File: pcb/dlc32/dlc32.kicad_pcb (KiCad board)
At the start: 2 copper layers, 46 x 79.2 mm, 55 parts, among them IC1 74LV11, IC2 74HCT08, IC3 MAX485E, IC4 AMS1117-3.3, IC5 74HCT04, J1 DOOR1, J10 TO_J7, J11 24V PWR, J12 LED LIGHTING, J13 AIR VALVE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

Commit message: Renumber, delete PCB.
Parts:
- removed C1, C2, C3, C4, C5, C6, C7: 100n, Capacitor_SMD:C_0805_2012Metric
- removed C10, C11, C8, C9: 100u, Capacitor_SMD:CP_Elec_10x10
- removed C12: 100n, Capacitor_SMD:C_0603_1608Metric
- removed D1: SS34, Diode_SMD:D_SMA
- removed IC1: 74LV11, Package_SO:SOIC-14_3.9x8.7mm_P1.27mm
- removed IC2: 74HCT08, Package_SO:SOIC-14_3.9x8.7mm_P1.27mm
- removed IC3: MAX485E, Package_SO:SOIC-8_3.9x4.9mm_P1.27mm
- removed IC4: AMS1117-3.3, Package_TO_SOT_SMD:SOT-223-3_TabPin2
- removed IC5: 74HCT04, Package_SO:SOIC-14_3.9x8.7mm_P1.27mm
- removed J1: DOOR1, Connector_JST:JST_PH_B3B-PH-K_1x03_P2.00mm_Vertical
- removed J10: TO_J7, Connector_JST:JST_XH_B06B-XH-A_1x06_P2.50mm_Vertical
- removed J11: 24V PWR, Connector_JST:JST_PH_B2B-PH-K_1x02_P2.00mm_Vertical
- removed J12: LED LIGHTING, Connector_JST:JST_PH_B2B-PH-K_1x02_P2.00mm_Vertical
- removed J13: AIR VALVE, Connector_JST:JST_PH_B2B-PH-K_1x02_P2.00mm_Vertical
- removed J14: AIMING LASER, Connector_JST:JST_PH_B2B-PH-K_1x02_P2.00mm_Vertical
- removed J15: CHILLER POWER, Connector_JST:JST_PH_B2B-PH-K_1x02_P2.00mm_Vertical
- removed J16: CHILLER SSR, Connector_JST:JST_PH_B2B-PH-K_1x02_P2.00mm_Vertical
- removed J2: DOOR2, Connector_JST:JST_PH_B3B-PH-K_1x03_P2.00mm_Vertical
- removed J3: CHILLER, Connector_JST:JST_PH_B2B-PH-K_1x02_P2.00mm_Vertical
- removed J4: TO_J8, Connector_JST:JST_XH_B06B-XH-A_1x06_P2.50mm_Vertical
- removed J5: POWEROFF, Connector_JST:JST_PH_B3B-PH-K_1x03_P2.00mm_Vertical
- removed J6: Conn_02x04_Odd_Even, Connector_PinSocket_2.54mm:PinSocket_2x04_P2.54mm_Vertical
- removed J7: LASER_AUX, Connector_JST:JST_PH_B5B-PH-K_1x05_P2.00mm_Vertical
- removed J8: LASER, Connector_JST:JST_PH_B5B-PH-K_1x05_P2.00mm_Vertical
- removed J9: CHILLER SERIAL, Connector_JST:JST_PH_B2B-PH-K_1x02_P2.00mm_Vertical
- removed LED1: Enable, LED_SMD:LED_0603_1608Metric
- removed Q1: ZXMN4A06, Package_TO_SOT_SMD:SOT-223-3_TabPin2
- removed R1, R2: 100, Resistor_SMD:R_0603_1608Metric
- removed R10: 120R, Resistor_SMD:R_0603_1608Metric
- removed R11, R13: 10K, Resistor_SMD:R_0603_1608Metric
- removed R12: 22R, Resistor_SMD:R_0603_1608Metric
- removed R3, R4, R5, R9: 1K, Resistor_SMD:R_0603_1608Metric
- removed R6, R7, R8: 5K6, Resistor_SMD:R_0603_1608Metric
- removed REF** (x4): MountingHole_3.2mm_M3, MountingHole:MountingHole_3.2mm_M3
- removed REF**: OSHW-Logo2_7.3x6mm_SilkScreen, Symbol:OSHW-Logo2_7.3x6mm_SilkScreen
- removed U1: MP1584 module, dlc32:MP1584-module
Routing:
- net GND: track 330.3 -> 0.00 mm, vias 6 -> 0
- net +5V: track 180.0 -> 0.00 mm, vias 6 -> 0
- net +3V3: track 135.8 -> 0.00 mm, vias 8 -> 0
- net RX: track 69.3 -> 0.00 mm, vias 4 -> 0
- net Net-(C11-Pad1): track 59.3 -> 0.00 mm
- net Net-(J3-Pad2): track 47.7 -> 0.00 mm, vias 1 -> 0
- net Net-(C10-Pad1): track 45.7 -> 0.00 mm, vias 1 -> 0
- net P2.12: track 44.7 -> 0.00 mm, vias 4 -> 0
- net Net-(J10-Pad4): track 43.2 -> 0.00 mm, vias 2 -> 0
- net Net-(IC2-Pad3): track 38.7 -> 0.00 mm, vias 2 -> 0
- net Net-(D1-Pad2): track 37.3 -> 0.00 mm
- net Net-(IC5-Pad2): track 36.7 -> 0.00 mm, vias 1 -> 0
- net P1.23: track 29.0 -> 0.00 mm, vias 3 -> 0
- net Net-(J2-Pad2): track 28.8 -> 0.00 mm, vias 2 -> 0
- net P4.28: track 23.9 -> 0.00 mm
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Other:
- board outline removed
- board text removed: "Lasersaur"
- board text removed: "https://github.com/bullestock/lasersaur/tree/master/pcb/msksbase"

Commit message: Start PCB.
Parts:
- added C1: 100n, Capacitor_SMD:C_0603_1608Metric, F.Cu at (96.5, 30.5)
- added C2: 100n, Capacitor_SMD:C_0603_1608Metric, F.Cu at (98.0, 47.7)
- added C3: 100n, Capacitor_SMD:C_0603_1608Metric, F.Cu at (98.0, 36.1)
- added C4: 100n, Capacitor_SMD:C_0603_1608Metric, F.Cu at (111.5, 37.3)
- added C5: 100n, Capacitor_SMD:C_0603_1608Metric, F.Cu at (111.5, 25.4)
- added C6: 100u, Capacitor_SMD:CP_Elec_10x10, F.Cu at (199.9, 30.2)
- added C7: 220u, Capacitor_SMD:CP_Elec_10x10, F.Cu at (95.5, 59.4)
- added C8: 100u, Capacitor_SMD:CP_Elec_10x10, F.Cu at (228.7, 101.3)
- added D1: SS34, Diode_SMD:D_SMA, F.Cu at (37.1, 143.3)
- added D2: LED, LED_THT:LED_D5.0mm_Horizontal_O1.27mm_Z3.0mm, F.Cu at (155.9, 47.3)
- added D3: LED, LED_THT:LED_D5.0mm_Horizontal_O1.27mm_Z3.0mm, F.Cu at (155.9, 55.8)
- added D4: LASER_ENABLE, LED_THT:LED_D5.0mm_Horizontal_O1.27mm_Z3.0mm, F.Cu at (155.9, 38.9)
- added D5: 1N4148, Diode_SMD:D_MiniMELF, F.Cu at (79.0, 63.2)
- added D6: LED, LED_THT:LED_D5.0mm_Horizontal_O1.27mm_Z3.0mm, F.Cu at (155.9, 64.3)
- added H1: MountingHole, MountingHole:MountingHole_3.2mm_M3, F.Cu at (78.0, 28.7)
- added H2: MountingHole, MountingHole:MountingHole_3.2mm_M3, F.Cu at (169.4, 28.7)
- added H3: MountingHole, MountingHole:MountingHole_3.2mm_M3, F.Cu at (78.0, 80.5)
- added H4: MountingHole, MountingHole:MountingHole_3.2mm_M3, F.Cu at (169.7, 80.5)
- added IC1: 74HCT08, Package_SO:SOIC-14_3.9x8.7mm_P1.27mm, F.Cu at (109.3, 31.0)
- added IC2: 74HCT04, Package_SO:SOIC-14_3.9x8.7mm_P1.27mm, F.Cu at (109.4, 42.9)
- added J1: DOOR1, Connector_JST:JST_XH_B4B-XH-A_1x04_P2.50mm_Vertical, F.Cu at (77.3, 37.3)
- added J10: VALVE/CHILLER SSR PWR, Connector_JST:JST_XH_B2B-XH-A_1x02_P2.50mm_Vertical, F.Cu at (186.2, 31.0)
- added J11: Conn_01x02, Connector_JST:JST_XH_B2B-XH-A_1x02_P2.50mm_Vertical, F.Cu at (199.4, 51.1)
- added J12: Conn_01x03, Connector_PinHeader_2.54mm:PinHeader_1x03_P2.54mm_Vertical, F.Cu at (90.5, 39.4)
- added J13: Conn_01x03, Connector_PinHeader_2.54mm:PinHeader_1x03_P2.54mm_Vertical, F.Cu at (94.6, 39.4)
- added J14: Conn_02x05_Odd_Even, Connector_IDC:IDC-Header_2x05_P2.54mm_Vertical, F.Cu at (240.3, 101.6)
- added J15: Conn_01x05, Connector_PinHeader_2.54mm:PinHeader_1x05_P2.54mm_Vertical, F.Cu at (249.7, 108.0)
- added J16: Conn_01x03, Connector_JST:JST_XH_B3B-XH-A_1x03_P2.50mm_Vertical, F.Cu at (102.2, 166.1)
- added J2: DOOR2, Connector_JST:JST_XH_B4B-XH-A_1x04_P2.50mm_Vertical, F.Cu at (77.3, 45.7)
- added J3: CHILLER_OK, Connector_JST:JST_XH_B2B-XH-A_1x02_P2.50mm_Vertical, F.Cu at (86.0, 29.1)
- added J4: CHILLER SWITCH, Connector_JST:JST_XH_B2B-XH-A_1x02_P2.50mm_Vertical, F.Cu at (45.3, 137.4)
- added J5: CHILLER SSR, Connector_JST:JST_XH_B2B-XH-A_1x02_P2.50mm_Vertical, F.Cu at (54.4, 137.4)
- added J6: AIR VALVE, Connector_JST:JST_XH_B2B-XH-A_1x02_P2.50mm_Vertical, F.Cu at (35.6, 137.4)
- added J7: LASER_AUX, Connector_JST:JST_XH_B5B-XH-A_1x05_P2.50mm_Vertical, F.Cu at (118.1, 29.2)
- added J8: LASER, Connector_JST:JST_XH_B5B-XH-A_1x05_P2.50mm_Vertical, F.Cu at (118.0, 36.6)
- added J9: AIMING LASER, Connector_JST:JST_XH_B2B-XH-A_1x02_P2.50mm_Vertical, F.Cu at (124.5, 117.1)
- added Q1: ZXMN4A06, Package_TO_SOT_SMD:SOT-223-3_TabPin2, F.Cu at (46.5, 145.3)
- added Q2: MMBT3904, Package_TO_SOT_SMD:SOT-23, F.Cu at (186.5, 49.3)
- added R1: 1K, Resistor_SMD:R_0603_1608Metric, F.Cu at (90.5, 35.3)
- added R10: R, Resistor_SMD:R_0603_1608Metric, F.Cu at (152.9, 47.2)
- added R11: 10K, Resistor_SMD:R_0603_1608Metric, F.Cu at (39.9, 146.1)
- added R12: 22R, Resistor_SMD:R_0603_1608Metric, F.Cu at (39.9, 148.1)
- added R13: 10K, Resistor_SMD:R_0603_1608Metric, F.Cu at (101.9, 33.5)
- added R14: R, Resistor_SMD:R_0603_1608Metric, F.Cu at (152.9, 53.3)
- added R15: 4k7, Resistor_SMD:R_0603_1608Metric, F.Cu at (85.1, 68.8)
- added R16: 100, Resistor_SMD:R_0603_1608Metric, F.Cu at (79.0, 57.4)
- added R17: 1M, Resistor_SMD:R_0603_1608Metric, F.Cu at (85.7, 58.7)
- added R18: 1k, Resistor_SMD:R_0603_1608Metric, F.Cu at (85.1, 63.8)
- added R19: 1k, Resistor_SMD:R_0603_1608Metric, F.Cu at (191.0, 48.3)
- added R2: 1K, Resistor_SMD:R_0603_1608Metric, F.Cu at (94.6, 35.3)
- added R20: R, Resistor_SMD:R_0603_1608Metric, F.Cu at (153.0, 61.7)
- added R3: 1K, Resistor_SMD:R_0603_1608Metric, F.Cu at (90.5, 48.5)
- added R4: 1K, Resistor_SMD:R_0603_1608Metric, F.Cu at (94.6, 48.5)
- added R5: 1K, Resistor_SMD:R_0603_1608Metric, F.Cu at (93.3, 31.2)
- added R6: 5K6, Resistor_SMD:R_0603_1608Metric, F.Cu at (98.0, 39.9)
- added R7: 5K6, Resistor_SMD:R_0603_1608Metric, F.Cu at (98.0, 43.7)
- added R8: 5K6, Resistor_SMD:R_0603_1608Metric, F.Cu at (93.3, 27.7)
- added R9: 1K, Resistor_SMD:R_0603_1608Metric, F.Cu at (153.0, 36.1)
- added RL1: G6B-1114C-US-DC5, hal9k:DIL-relay, F.Cu at (185.7, 45.3)
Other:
- board outline added: 99.8 x 60.2 mm

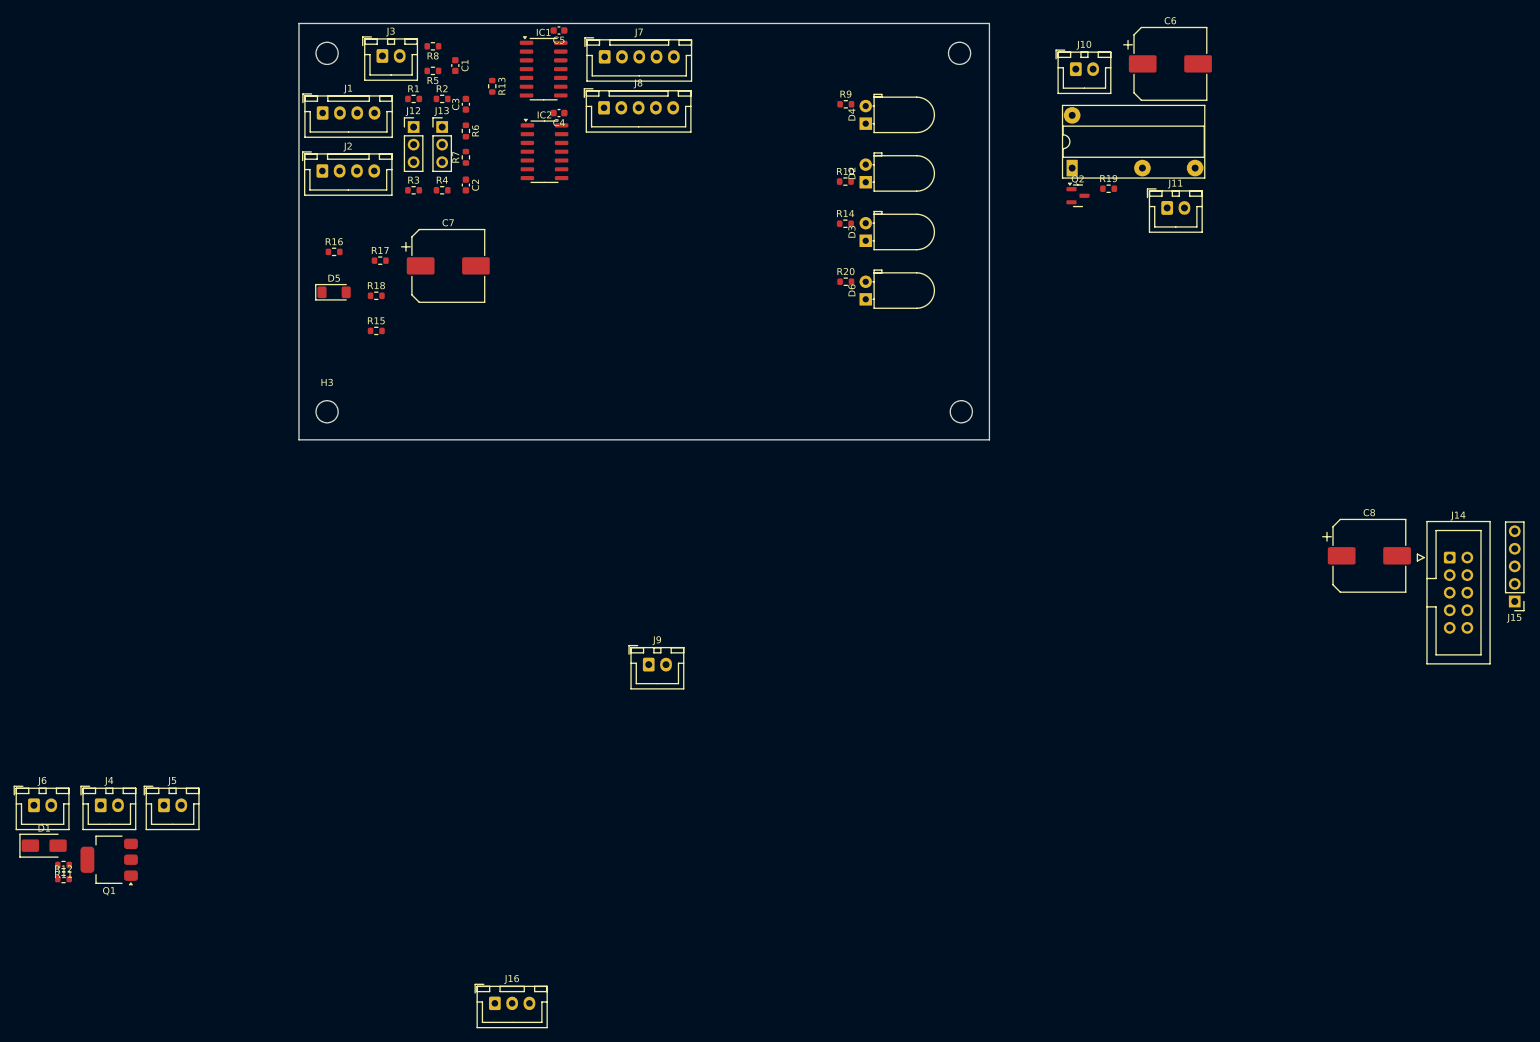
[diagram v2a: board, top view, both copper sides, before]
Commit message: Use resistor array.
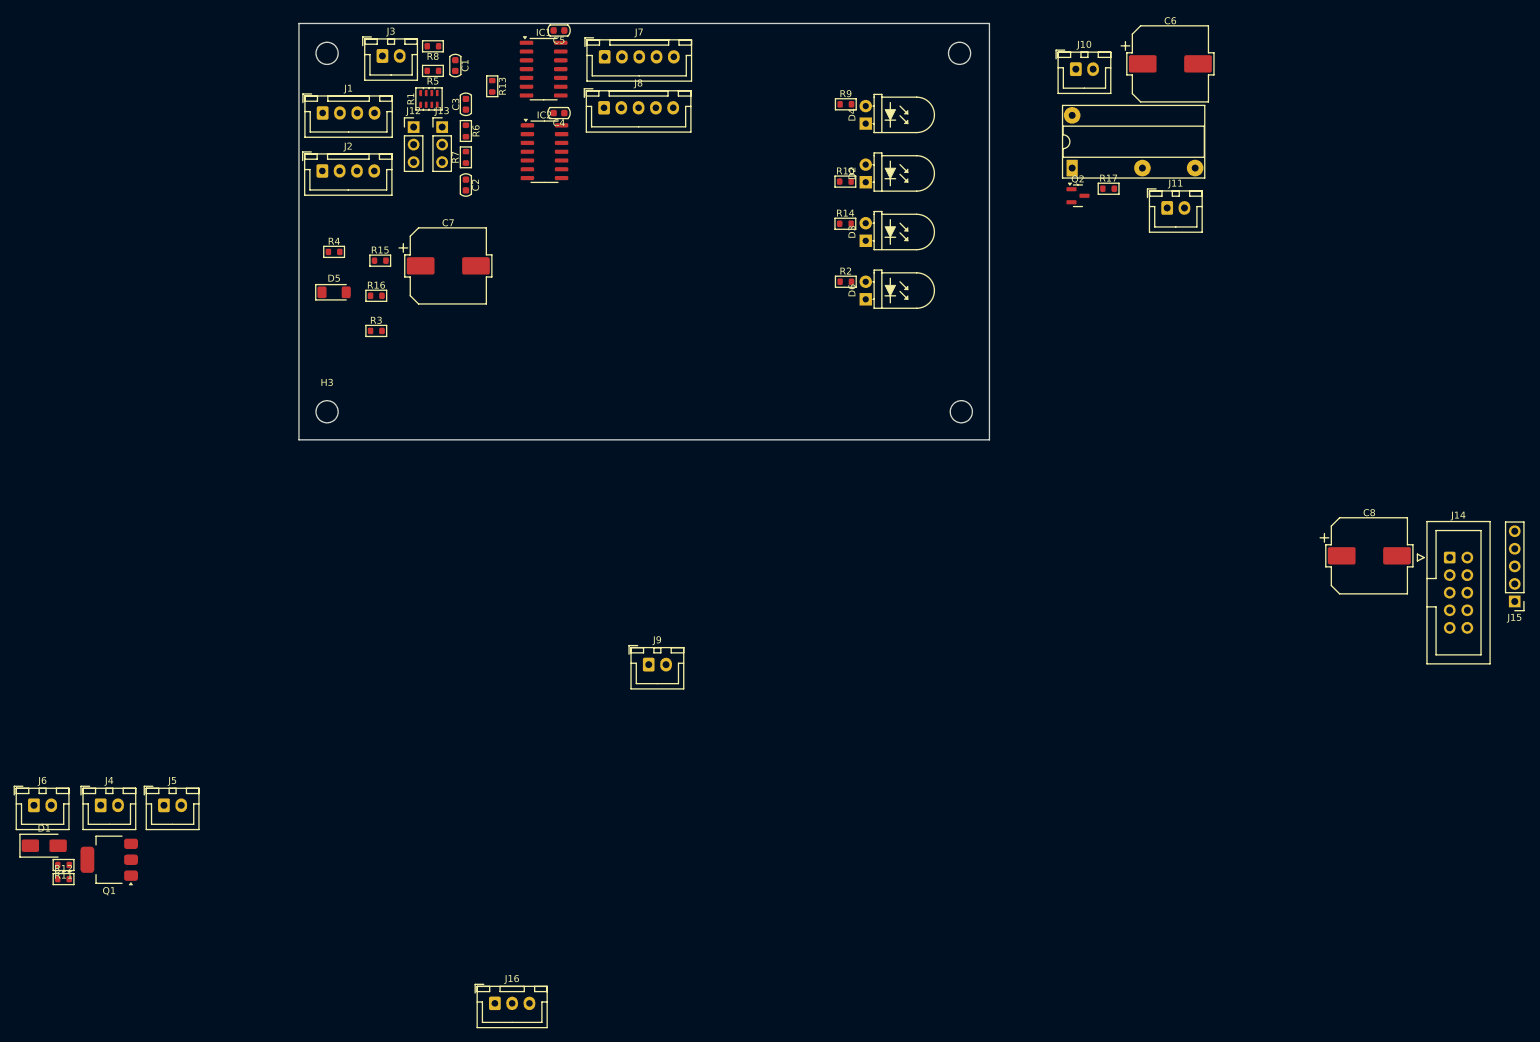
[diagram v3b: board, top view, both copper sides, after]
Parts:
- removed the R2 at (94.6, 35.3)
- removed the R3 at (90.5, 48.5)
- removed the R4 at (94.6, 48.5)
- C1, C2, C3, C4, C5: footprint Capacitor_SMD:C_0603_1608Metric -> PCM_Capacitor_SMD_AKL:C_0603_1608Metric
- C6, C7, C8: footprint Capacitor_SMD:CP_Elec_10x10 -> PCM_Capacitor_SMD_AKL:CP_Elec_10x10
- D2, D3, D4, D6: footprint LED_THT:LED_D5.0mm_Horizontal_O1.27mm_Z3.0mm -> PCM_LED_THT_AKL:LED_D5.0mm_Horizontal_O1.27mm_Z3.0mm
- R1: footprint Resistor_SMD:R_0603_1608Metric -> PCM_Resistor_SMD_AKL:R_Array_Concave_4x0603
- R10, R14: value R -> 2K7; footprint Resistor_SMD:R_0603_1608Metric -> PCM_Resistor_SMD_AKL:R_0603_1608Metric
- R11, R12, R13, R5, R6, R7, R8, R9: footprint Resistor_SMD:R_0603_1608Metric -> PCM_Resistor_SMD_AKL:R_0603_1608Metric
- R15: renamed from R17; footprint Resistor_SMD:R_0603_1608Metric -> PCM_Resistor_SMD_AKL:R_0603_1608Metric
- R16: renamed from R18; footprint Resistor_SMD:R_0603_1608Metric -> PCM_Resistor_SMD_AKL:R_0603_1608Metric
- R17: renamed from R19; footprint Resistor_SMD:R_0603_1608Metric -> PCM_Resistor_SMD_AKL:R_0603_1608Metric
- R2: renamed from R20; footprint Resistor_SMD:R_0603_1608Metric -> PCM_Resistor_SMD_AKL:R_0603_1608Metric
- R3: renamed from R15; footprint Resistor_SMD:R_0603_1608Metric -> PCM_Resistor_SMD_AKL:R_0603_1608Metric
- R4: renamed from R16; footprint Resistor_SMD:R_0603_1608Metric -> PCM_Resistor_SMD_AKL:R_0603_1608Metric
- moved R1 2.22 mm to (92.7, 35.3), turned to 90 degrees
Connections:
- J12 pad 2: Net-(J1-Pin_2) -> Net-(J12-Pin_2)
- J13 pad 2: Net-(J13-Pin_2) -> Net-(J12-Pin_2)
- J2 pad 2: Net-(J13-Pin_2) -> Net-(J12-Pin_2)
- R1 pad 1: +5V -> Net-(J12-Pin_1)
- R1 pad 2: Net-(J12-Pin_1) -> Net-(J12-Pin_3)
- R14 pad 2: Net-(C1-Pad1) -> Net-(J3-Pin_2)
- R7 pad 2: Net-(J13-Pin_2) -> Net-(J12-Pin_2)

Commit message: Add optional +5V power, route.
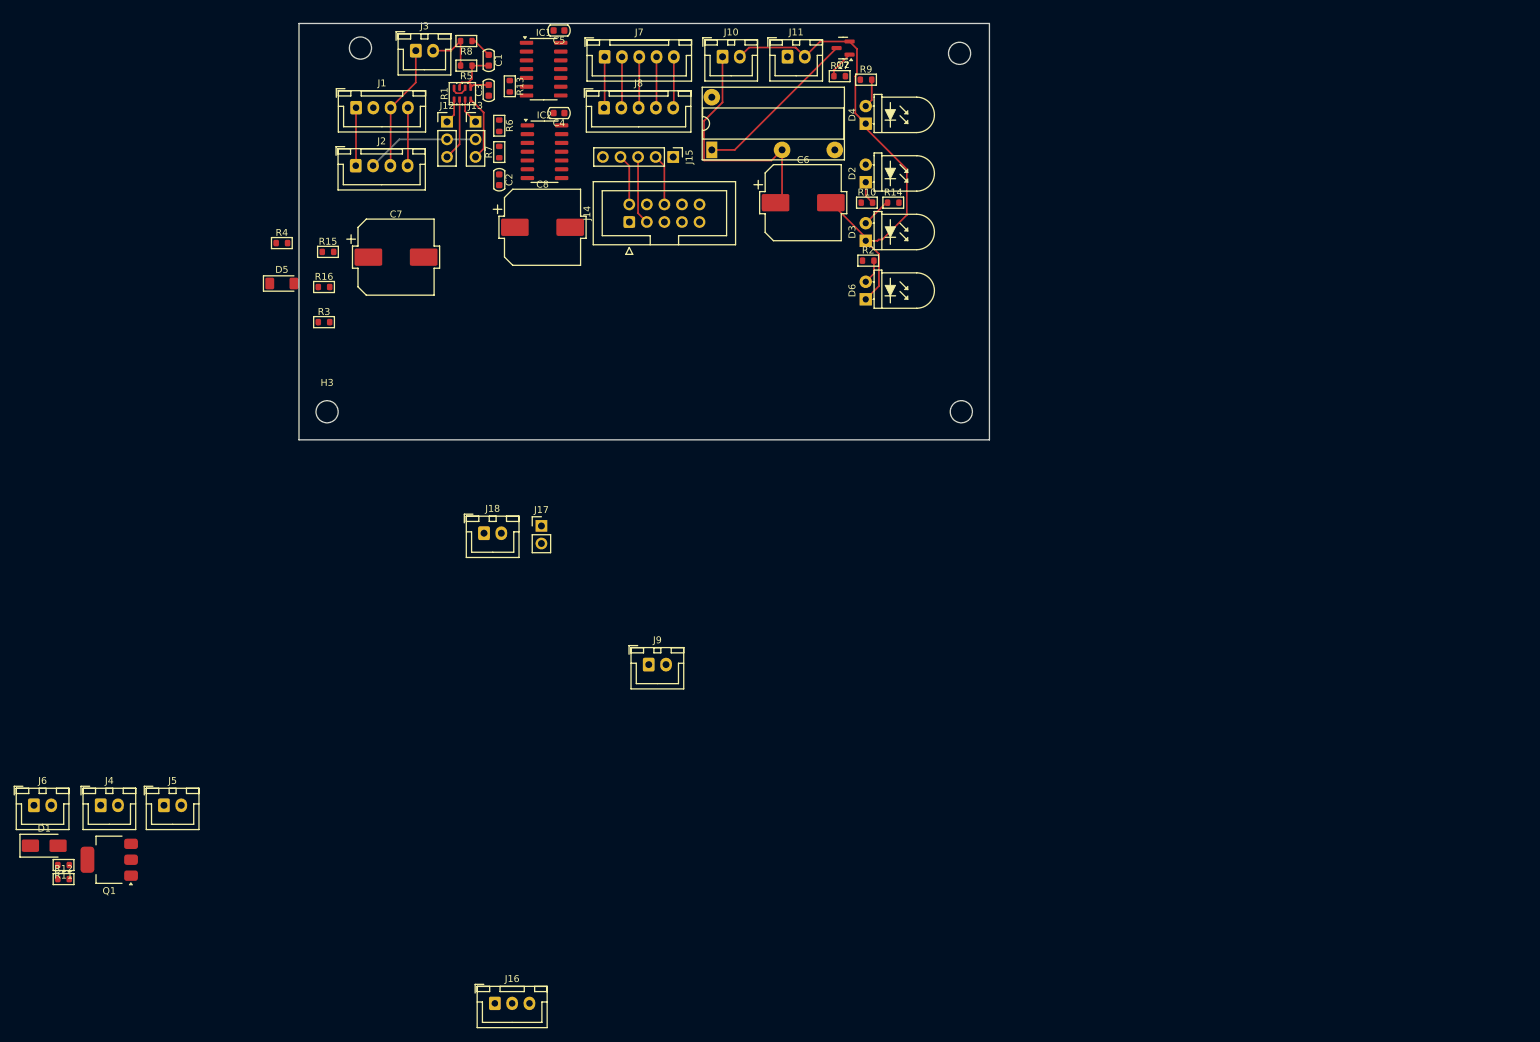
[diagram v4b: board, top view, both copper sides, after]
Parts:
- added J17: Conn_01x02, Connector_PinHeader_2.54mm:PinHeader_1x02_P2.54mm_Vertical, F.Cu at (109.0, 97.0)
- added J18: Conn_01x02, Connector_JST:JST_XH_B2B-XH-A_1x02_P2.50mm_Vertical, F.Cu at (100.7, 98.1)
- moved J15 137.6 mm to (128.0, 43.7), turned to -90 degrees
- moved C8 128.6 mm to (109.1, 53.8)
- moved J14 128.2 mm to (121.7, 53.1), turned to 90 degrees
- moved J11 59.1 mm to (144.5, 29.2)
- moved C6 56.8 mm to (146.8, 50.3)
- moved RL1 52.2 mm to (133.6, 42.7)
- moved J10 51.1 mm to (135.1, 29.2)
- moved R17 42.1 mm to (152.1, 32.0)
- moved Q2 40.1 mm to (152.6, 27.9), turned to 180 degrees
- moved C7 7.66 mm to (87.9, 58.2)
- moved R3 7.66 mm to (77.5, 67.6)
- moved D5 7.66 mm to (71.4, 62.0)
- moved R4 7.66 mm to (71.4, 56.1)
- moved R15 7.66 mm to (78.1, 57.4)
- moved R16 7.66 mm to (77.5, 62.5)
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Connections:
- J14 pad 1: +5V -> Net-(J14-Pin_1)
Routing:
- net GND: track 0.00 -> 105.5 mm
- net +V_VALVE: track 0.00 -> 44.4 mm
- net +5V: track 0.00 -> 28.2 mm
- net Net-(Q2-C): track 0.00 -> 24.1 mm
- net Net-(J12-Pin_2): track 0.00 -> 16.4 mm
- net RX: track 0.00 -> 9.92 mm
- net Net-(J13-Pin_3): track 0.00 -> 9.56 mm
- net Net-(J12-Pin_3): track 0.00 -> 9.05 mm
- net Net-(J3-Pin_2): track 0.00 -> 8.11 mm
- net Net-(J7-Pin_4): track 0.00 -> 7.40 mm
- net Net-(J7-Pin_3): track 0.00 -> 7.40 mm
- net Net-(J7-Pin_2): track 0.00 -> 7.40 mm
- net TX: track 0.00 -> 7.38 mm
- net Net-(D3-A): track 0.00 -> 4.38 mm
- net Net-(D4-A): track 0.00 -> 4.17 mm
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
